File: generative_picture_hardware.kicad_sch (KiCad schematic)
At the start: 3 parts

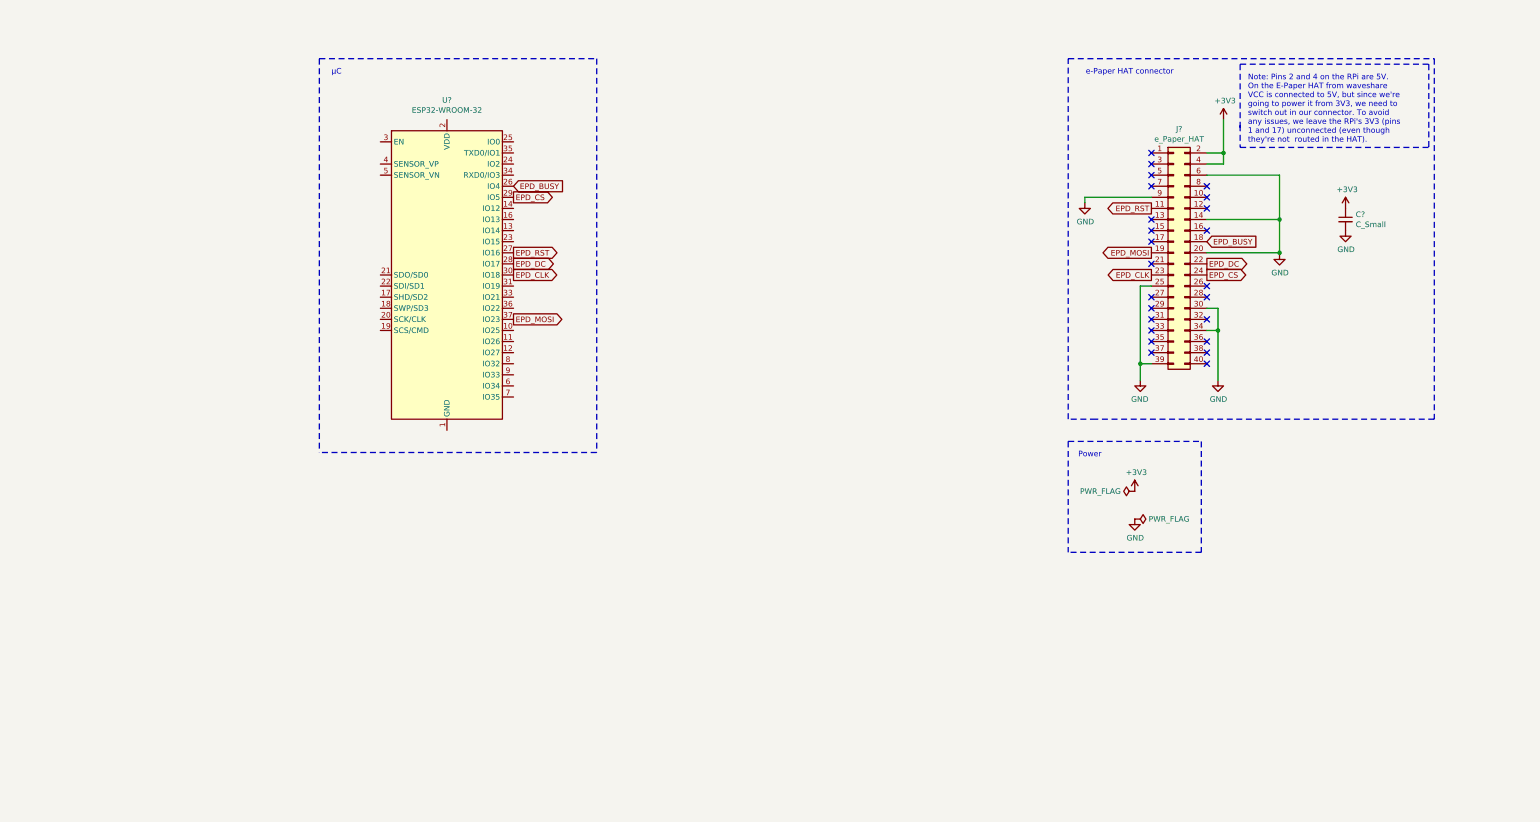
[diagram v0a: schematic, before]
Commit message: Adds JTAG connector
I'm using 100Ω series resistors in the JTAG lines as per the reference
design in the ESP32-WROOM-32 datasheet[1] (section 7).

[1]: https://www.espressif.com/sites/default/files/documentation/esp32-wroom-32_datasheet_en.pdf
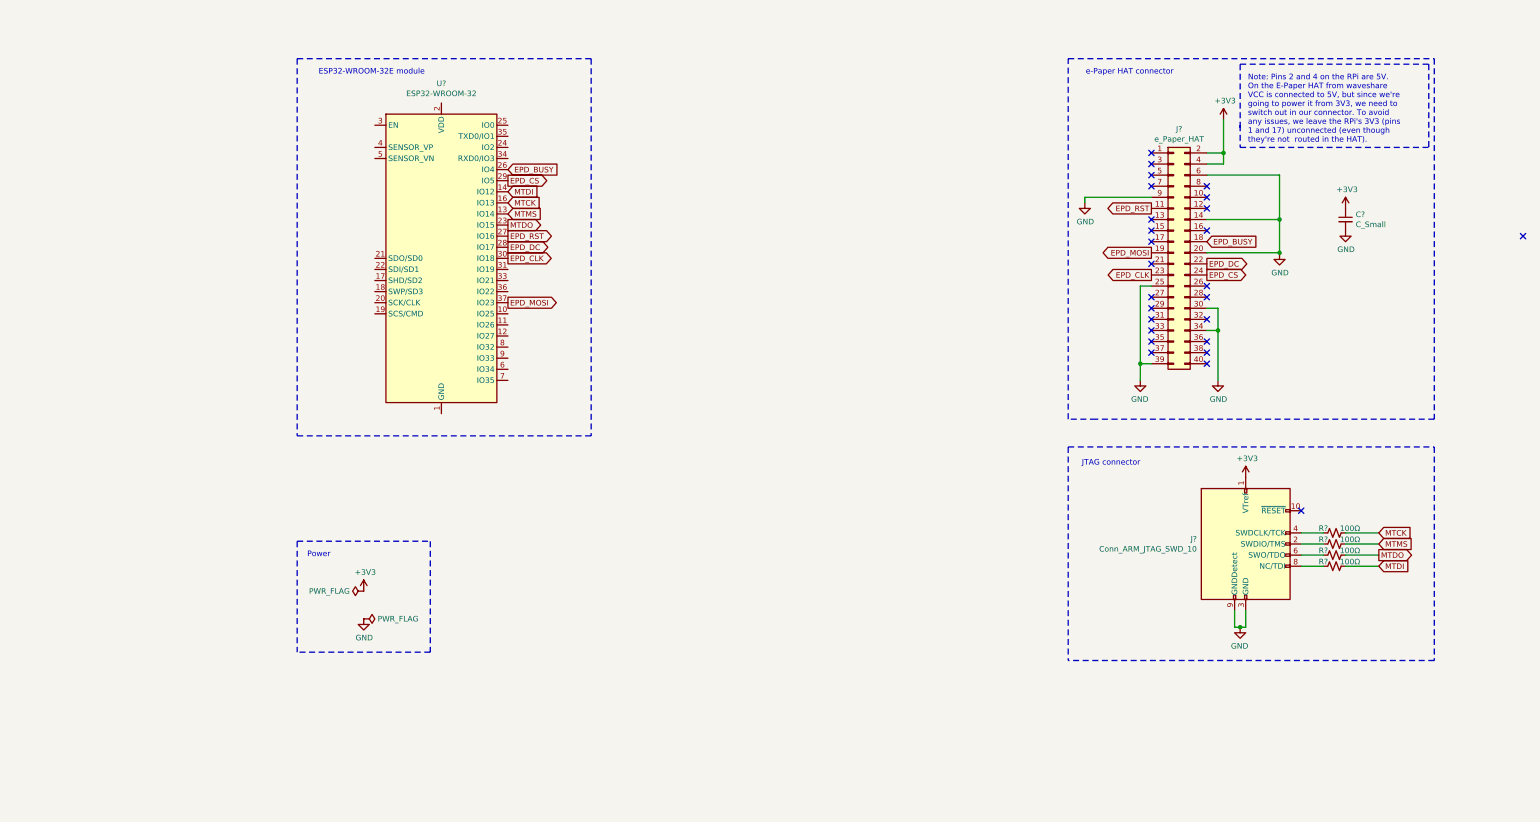
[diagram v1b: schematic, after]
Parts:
- added J?: Conn_ARM_JTAG_SWD_10, symbol Connector:Conn_ARM_JTAG_SWD_10
- added R? (x4): 100Ω, symbol Device:R_Small_US
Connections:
- net +3V3: now also J?.1 (VTref)
- net GND: now also J?.3 (GND), J?.5 (GND), J?.9 (GNDDetect)
- net MTMS: now reaches U?.13 (IO14)
- net MTMS: now also R?.2
- net MTDI: now reaches U?.14 (IO12)
- net MTDI: now also R?.2
- net MTCK: now reaches U?.16 (IO13)
- net MTCK: now also R?.2
- net MTDO: now reaches U?.23 (IO15)
- net MTDO: now also R?.2
- new net: J?.2 (SWDIO/TMS), R?.1
- new net: J?.4 (SWDCLK/TCK), R?.1
- new net: J?.6 (SWO/TDO), R?.1
- new net: J?.8 (NC/TDI), R?.1
- no-connect marks 24 -> 26
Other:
- note added: "ESP32-WROOM-32E module"
- note added: "JTAG connector"
- note removed: "µC"
- moved on the sheet: U?

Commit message: Adds minimal circuit around the ESP32 module
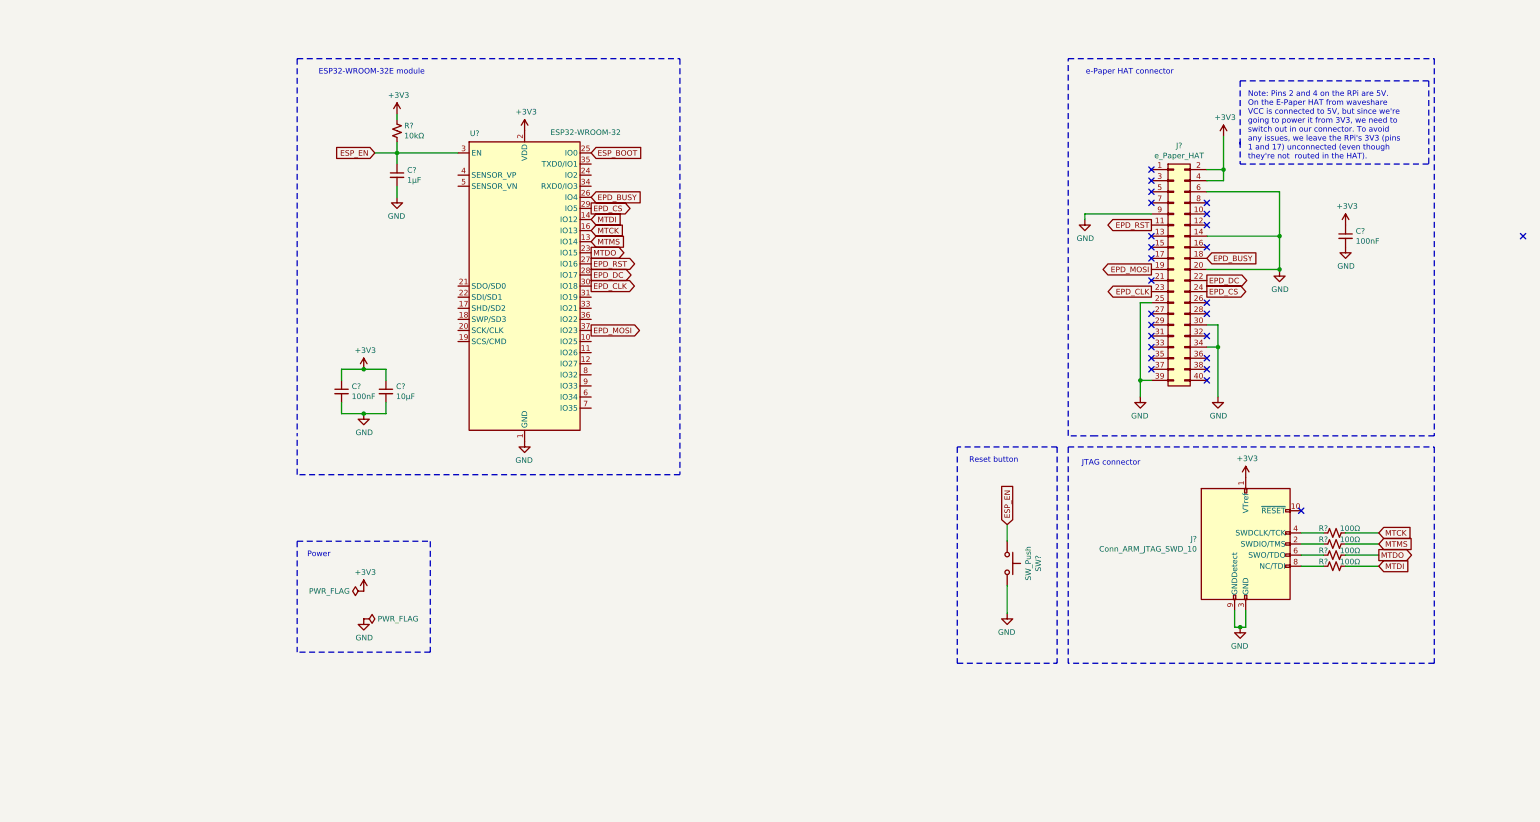
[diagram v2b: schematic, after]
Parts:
- added C?: 1µF, symbol Device:C_Small
- added C?: 10µF, symbol Device:C_Small
- added C?: 100nF, symbol Device:C_Small
- added R?: 10kΩ, symbol Device:R_Small_US
- added SW?: SW_Push, symbol Switch:SW_Push
- C?: value C_Small -> 100nF
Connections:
- net +3V3: now also U?.2 (VDD), C?.1, C?.1, R?.1
- net GND: now also U?.1 (GND), U?.15 (GND), U?.38 (GND), U?.39 (GND), C?.2, C?.2, C?.2, SW?.2
- net ESP_BOOT: now reaches U?.25 (IO0)
- net ESP_EN: now reaches U?.3 (EN)
- net ESP_EN: now also C?.1, R?.2, SW?.1
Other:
- note added: "Reset button"
- moved on the sheet: C?, J?, U?

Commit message: Adds USB to UART converter and auto-reset circuit
I'm using the FTDI FT231XS USB to UART converter IC. There's also a
TVS diode array for ESD protection, which might be overkill but I
decided to add it anyways.
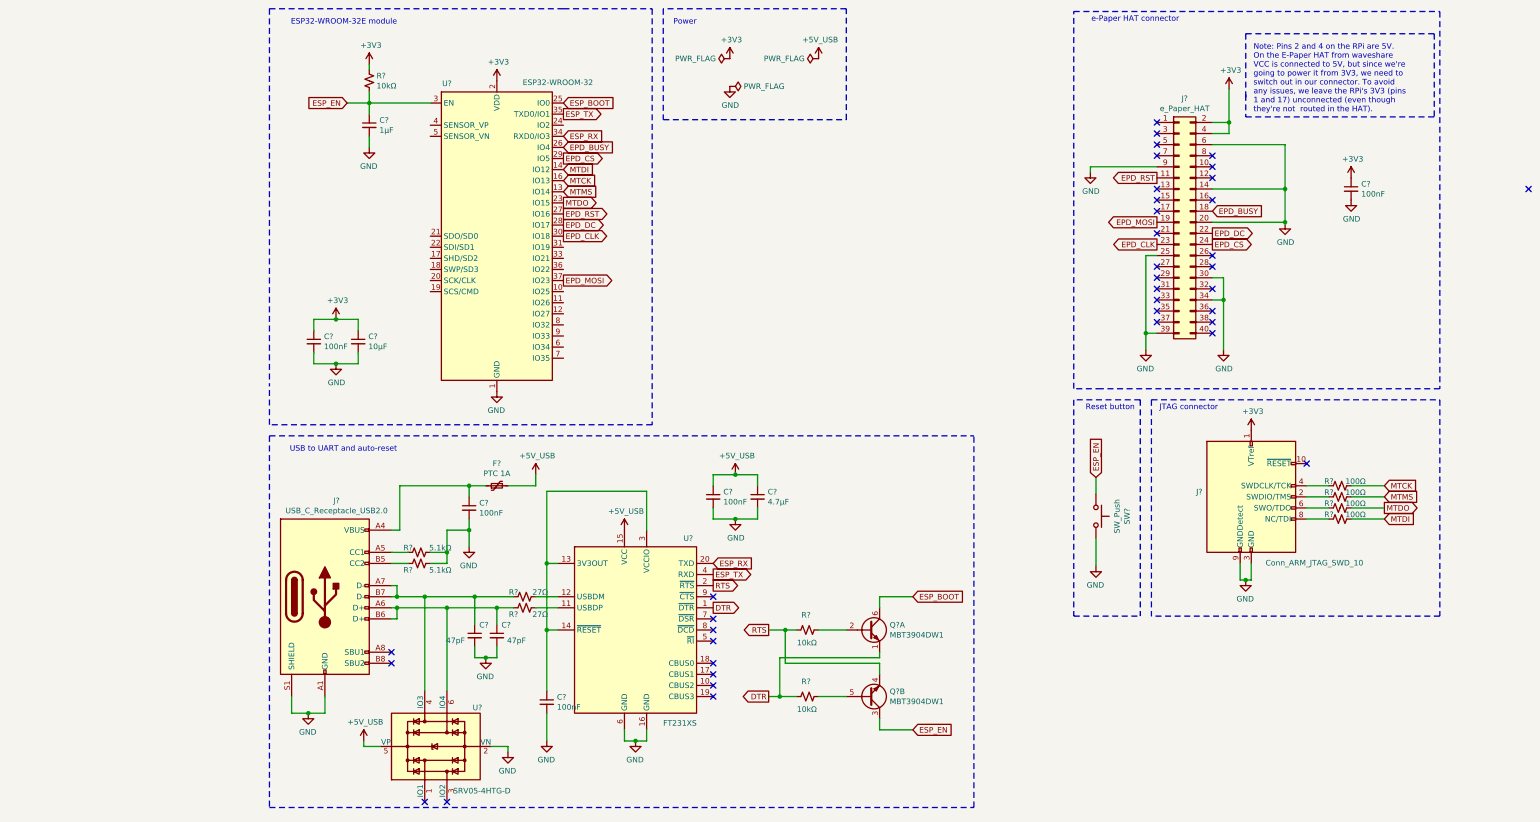
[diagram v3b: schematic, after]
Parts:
- added C?: 4.7µF, symbol Device:C_Small
- added C? (x3): 100nF, symbol Device:C_Small
- added C? (x2): 47pF, symbol Device:C_Small
- added F?: PTC 1A, symbol Device:Polyfuse_Small
- added J?: USB_C_Receptacle_USB2.0, symbol Connector:USB_C_Receptacle_USB2.0
- added Q? (x2): MBT3904DW1, Package_TO_SOT_SMD:SOT-363_SC-70-6, symbol Transistor_BJT:MBT3904DW1
- added R? (x2): 27Ω, symbol Device:R_Small_US
- added R? (x2): 10kΩ, symbol Device:R_Small_US
- added R? (x2): 5.1kΩ, symbol Device:R_Small_US
- added U?: FT231XS, Package_SO:SSOP-20_3.9x8.7mm_P0.635mm, symbol Interface_USB:FT231XS
- added U?: SRV05-4HTG-D, Package_TO_SOT_SMD:SOT-23-6, symbol Power_Protection:SRV05-4
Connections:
- net ESP_BOOT: now also Q?.6 (C1)
- net ESP_EN: now also Q?.3 (C2)
- net GND: now also C?.2, C?.2, C?.2, C?.2, C?.2, C?.2, J?.A1 (GND), J?.A12 (GND), J?.B1 (GND), J?.B12 (GND), J?.S1 (SHIELD), R?.2, R?.2, U?.16 (GND), U?.2 (VN), U?.6 (GND)
- net ESP_RX: now reaches U?.34 (RXD0/IO3)
- net ESP_RX: now also U?.20 (TXD)
- net ESP_TX: now reaches U?.35 (TXD0/IO1)
- net ESP_TX: now also U?.4 (RXD)
- new net: C?.1, J?.A7 (D-), J?.B7 (D-), R?.1, U?.4 (IO3)
- new net: R?.2, U?.12 (USBDM)
- new net: C?.1, F?.1, J?.A4 (VBUS), J?.A9 (VBUS), J?.B4 (VBUS), J?.B9 (VBUS)
- new net: J?.A5 (CC1), R?.1
- new net: C?.1, J?.A6 (D+), J?.B6 (D+), R?.1, U?.6 (IO4)
- new net: J?.B5 (CC2), R?.1
- new net: C?.1, U?.13 (3V3OUT), U?.14 (~RESET), U?.3 (VCCIO)
- new net: Q?.5 (B2), R?.1
- new net: Q?.2 (B1), R?.1
- new net: R?.2, U?.11 (USBDP)
- new net +5V: C?.1, C?.1, F?.2, U?.15 (VCC), U?.5 (VP)
- new net DTR: Q?.1 (E1), R?.2, U?.1 (~DTR)
- new net RTS: Q?.4 (E2), R?.2, U?.2 (~RTS)
- no-connect marks 26 -> 38
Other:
- note added: "USB to UART and auto-reset"
- moved on the sheet: C?, J?, R?, SW?, U?

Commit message: Adds boot button and fixes global label directions
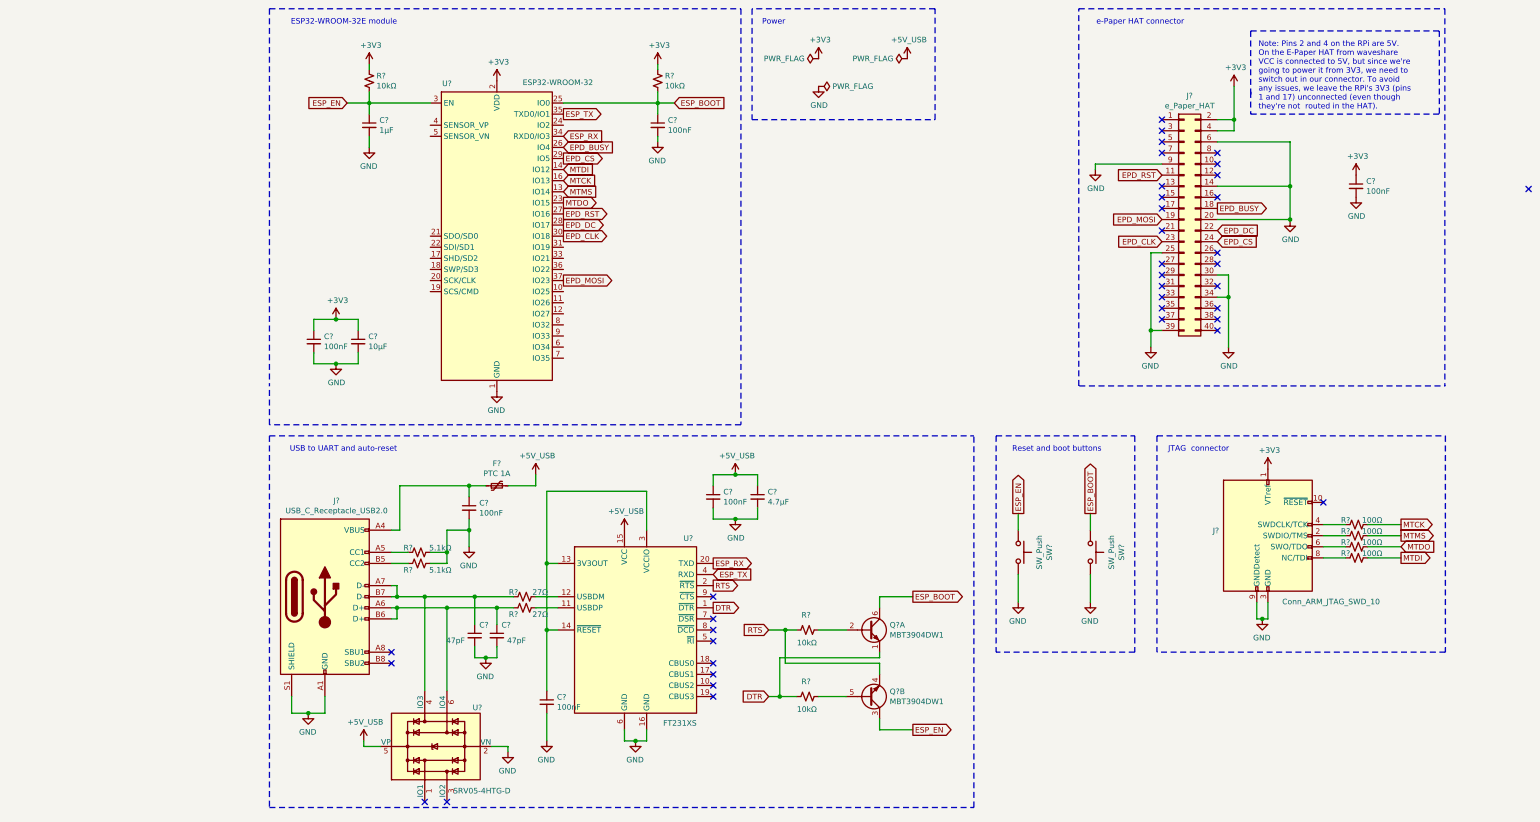
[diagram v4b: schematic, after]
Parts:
- added C?: 100nF, symbol Device:C_Small
- added R?: 10kΩ, symbol Device:R_Small_US
- added SW?: SW_Push, symbol Switch:SW_Push
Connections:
- net +3V3: now also R?.1
- net ESP_BOOT: now also C?.1, R?.2, SW?.1
- net GND: now also C?.2, SW?.2
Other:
- note added: "Reset and boot buttons"
- note removed: "Reset button"
- moved on the sheet: C?, J?, R?, SW?

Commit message: Adds LiPo charging circuit
Uses the MCP73831 to charge a single cell LiPo battery that should
have undervoltage protection builtin[1]

[1]: Such as https://www.adafruit.com/product/328
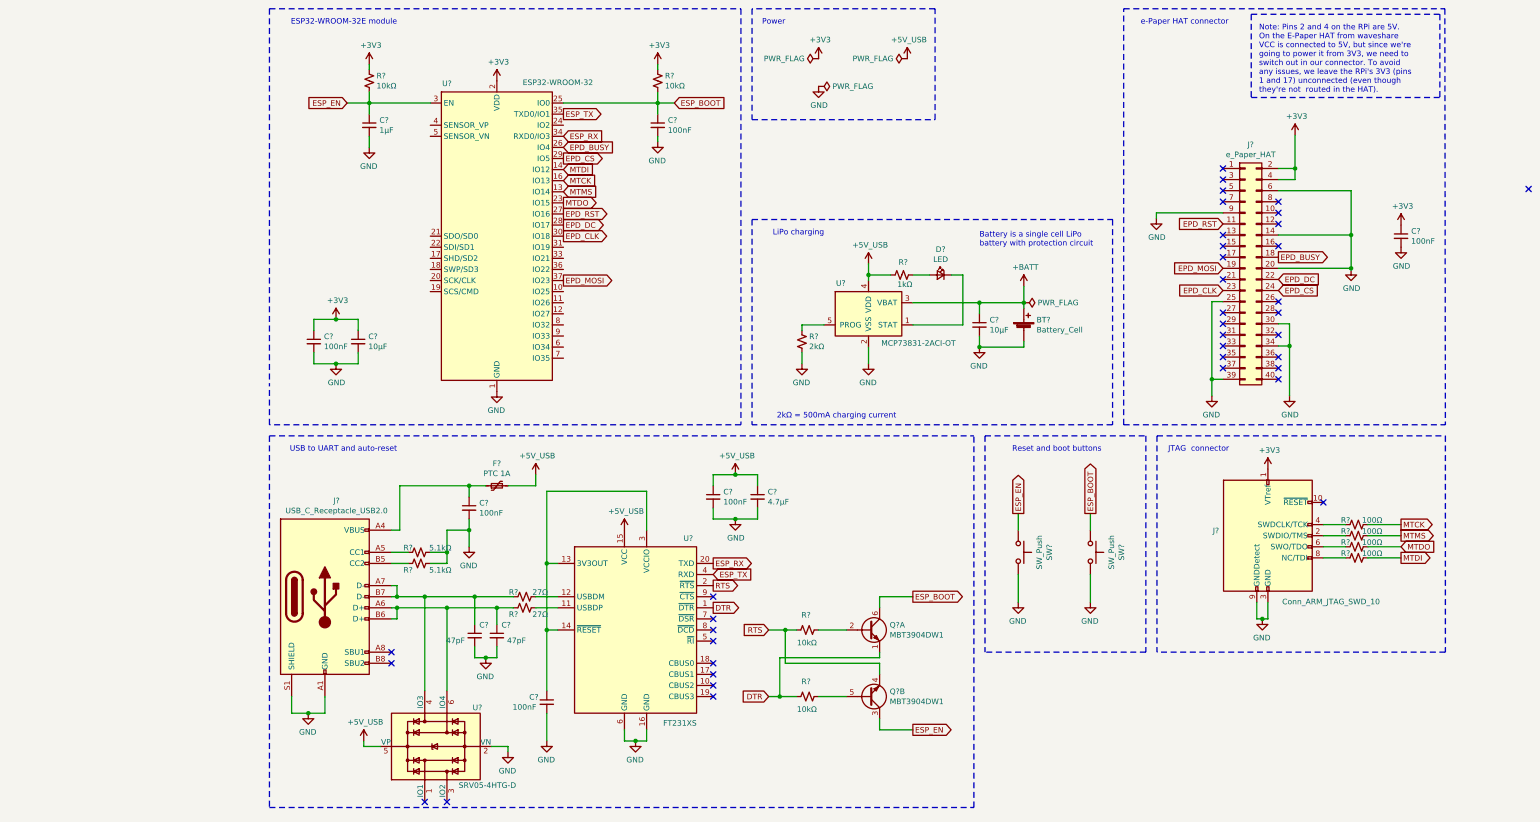
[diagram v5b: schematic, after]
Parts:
- added BT?: Battery_Cell, symbol Device:Battery_Cell
- added C?: 10µF, symbol Device:C_Small
- added D?: LED, symbol Device:LED_Small
- added R?: 2kΩ, symbol Device:R_Small_US
- added R?: 1kΩ, symbol Device:R_Small_US
- added U?: MCP73831-2ACI-OT, Package_TO_SOT_SMD:SOT-23-5, symbol Battery_Management:MCP73831-2-OT
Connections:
- net +5V: now also R?.1, U?.4 (VDD)
- net GND: now also BT?.2 (-), C?.2, R?.2, U?.2 (VSS)
- new net: D?.1 (K), U?.1 (STAT)
- new net: R?.1, U?.5 (PROG)
- new net: D?.2 (A), R?.2
- new net +BATT: BT?.1 (+), C?.1, U?.3 (VBAT)
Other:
- note added: "2kΩ = 500mA charging current"
- note added: "Battery is a single cell LiPo battery with protection circuit"
- note added: "LiPo charging"
- moved on the sheet: C?, J?
